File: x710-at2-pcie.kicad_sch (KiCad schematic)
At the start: 16 parts, among them J3 PinHeader_2x3_P2.54mm_SMD, U4 EZX710AT2_S_LMR5

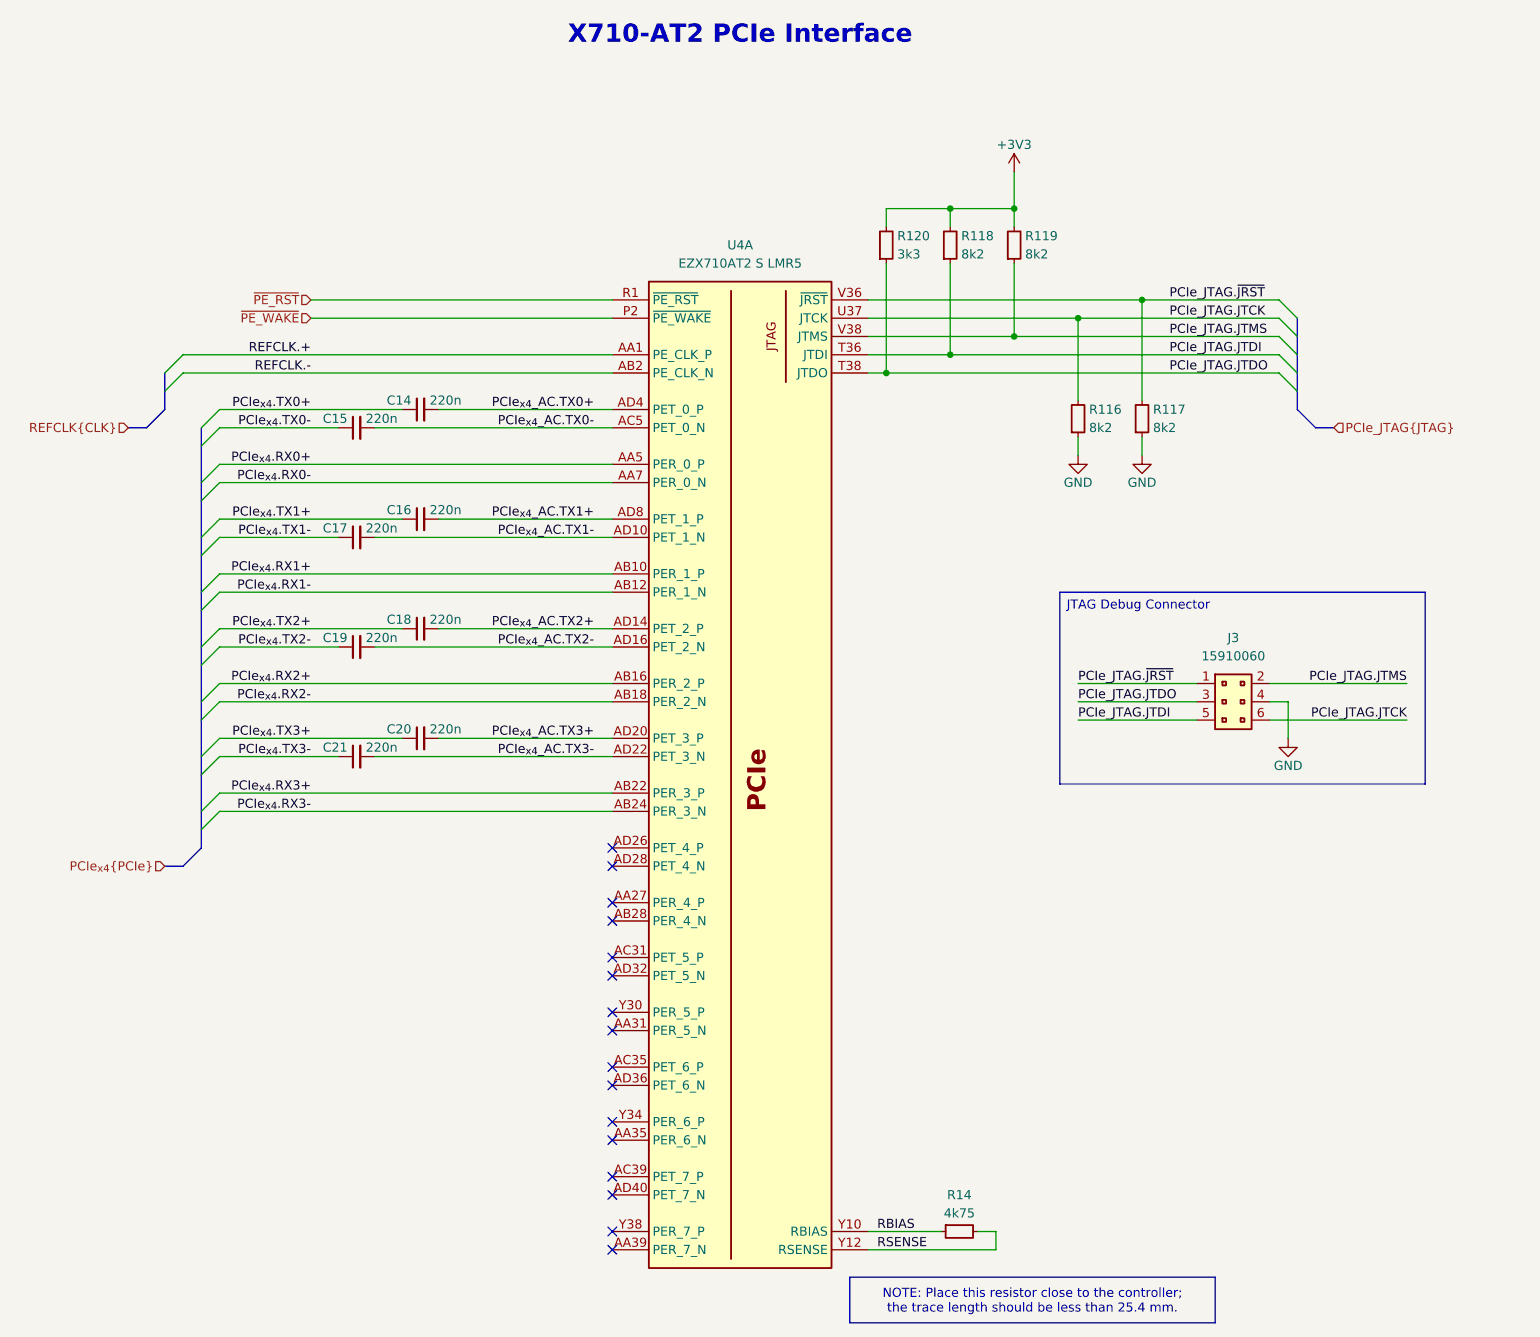
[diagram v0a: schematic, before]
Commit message: [#80813] Add OCuLink connector
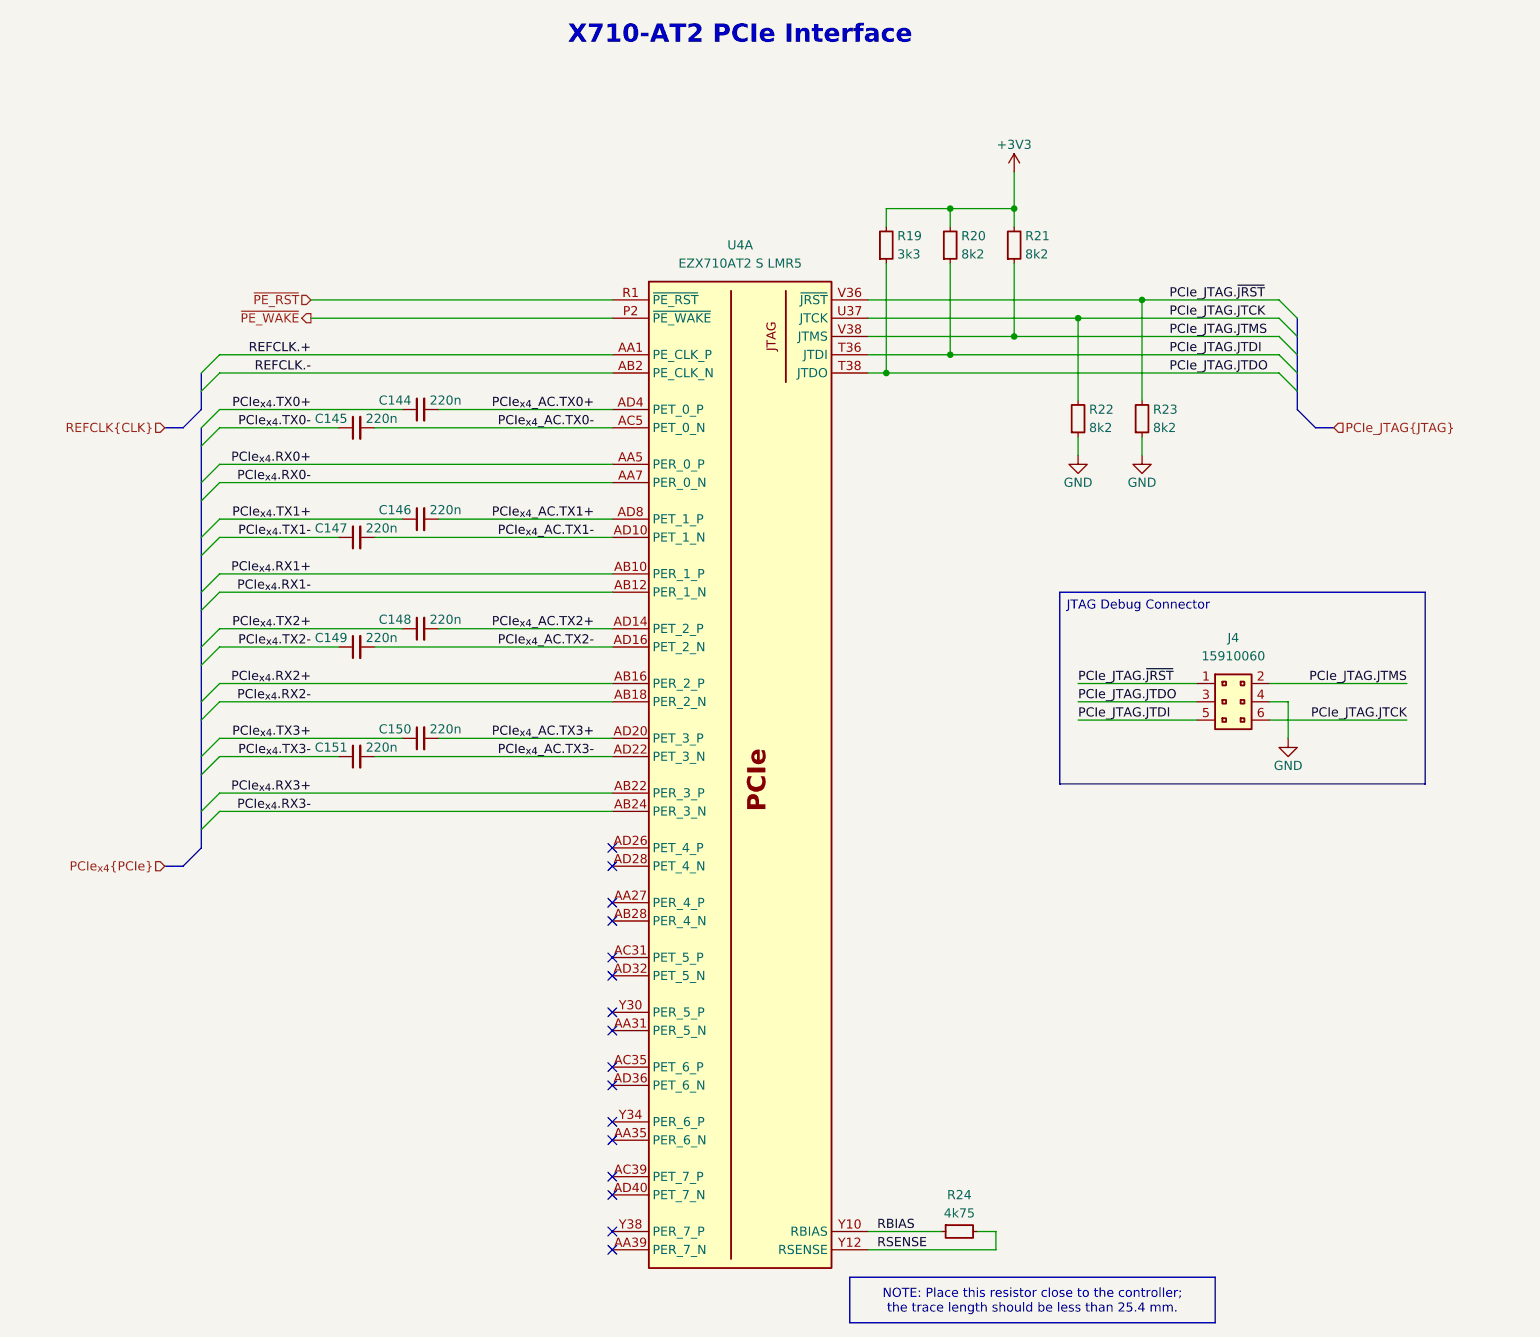
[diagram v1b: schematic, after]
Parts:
- renumbered C14 to C144, C15 to C145, C16 to C146, C17 to C147, C18 to C148, C19 to C149, C20 to C150, C21 to C151, J3 to J4, R120 to R19, R118 to R20, R119 to R21, R116 to R22, R117 to R23, R14 to R24
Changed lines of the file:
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@@
 	)
 	(bus_alias "PCIe"
-		(members "TX7+" "TX7-" "TX6+" "TX6-" "TX5+" "TX5-" "TX4+" "TX4-" "TX3+"
-			"TX3-" "TX2+" "TX2-" "TX1+" "TX1-" "TX0+" "TX0-" "RX7+" "RX7-" "RX6+"
-			"RX6-" "RX5+" "RX5-" "RX4+" "RX4-" "RX3+" "RX3-" "RX2+" "RX2-" "RX1+"
-			"RX1-" "RX0+" "RX0-"
+		(members "TX3+" "TX3-" "TX2+" "TX2-" "TX1+" "TX1-" "TX0+" "TX0-" "RX3+"
+			"RX3-" "RX2+" "RX2-" "RX1+" "RX1-" "RX0+" "RX0-"
 		)
 	)
@@
 	)
 	(bus_entry
-		(at 135.89 97.79)
+		(at 140.97 97.79)
 		(size 2.54 -2.54)
 		(stroke
@@
 	)
 	(bus_entry
-		(at 135.89 100.33)
+		(at 140.97 100.33)
 		(size 2.54 -2.54)
 		(stroke
@@
 	(bus
 		(pts
-			(xy 135.89 97.79) (xy 135.89 100.33)
+			(xy 140.97 97.79) (xy 140.97 100.33)
 		)
 		(stroke
@@
 	(bus
 		(pts
-			(xy 135.89 100.33) (xy 135.89 102.87)
+			(xy 140.97 100.33) (xy 140.97 102.87)
 		)
 		(stroke
@@
 	(wire
 		(pts
-			(xy 138.43 97.79) (xy 198.12 97.79)
+			(xy 143.51 97.79) (xy 198.12 97.79)
 		)
 		(stroke
@@
 	(wire
 		(pts
-			(xy 138.43 95.25) (xy 198.12 95.25)
+			(xy 143.51 95.25) (xy 198.12 95.25)
 		)
 		(stroke
@@
 	(bus
 		(pts
-			(xy 130.81 105.41) (xy 133.35 105.41)
+			(xy 135.89 105.41) (xy 138.43 105.41)
 		)
 		(stroke
@@
 	(bus
 		(pts
-			(xy 133.35 105.41) (xy 135.89 102.87)
+			(xy 138.43 105.41) (xy 140.97 102.87)
 		)
 		(stroke
@@
 	(hierarchical_label "REFCLK{CLK}"
 		(shape input)
-		(at 130.81 105.41 180)
+		(at 135.89 105.41 180)
 		(effects
 			(font
@@
 	)
 	(hierarchical_label "~{PE_WAKE}"
-		(shape input)
+		(shape output)
 		(at 156.21 90.17 180)
 		(effects
@@
 		(polyline
 			(pts
-				(xy 138.43 92.71) (xy 196.85 92.71) (xy 196.85 160.02) (xy 138.43 160.02)
+				(xy 139.7 92.71) (xy 196.85 92.71) (xy 196.85 160.02) (xy 139.7 160.02)
 			)
 			(stroke
@@
 		(length 2.54)
 		(shape round)
-		(at 138.43 92.71 0)
+		(at 139.7 92.71 0)
 		(fields_autoplaced yes)
 		(effects
@@
 		)
 		(property "Netclass" "85Ohm-diff_PCIe"
-			(at 137.7315 90.17 0)
+			(at 139.0015 90.17 0)
 			(effects
 				(font
@@
 		)
 		(property "Component Class" ""
-			(at -85.09 39.37 0)
+			(at -83.82 39.37 0)
 			(effects
 				(font
@@
 		(dnp no)
 		(fields_autoplaced yes)
-		(property "Reference" "J3"
+		(property "Reference" "J4"
 			(at 284.48 134.62 0)
 			(effects
@@
 			(project "10-gbe-expansion"
 				(path "/04bda987-e5eb-48b4-9e90-d8211dc11b39/2e3e9f9b-8e60-4e62-87df-aa866913a2fb"
-					(reference "J3")
+					(reference "J4")
 					(unit 1)
 				)
@@
 		(on_board yes)
 		(dnp no)
-		(property "Reference" "R119"
+		(property "Reference" "R21"
 			(at 255.524 78.74 90)
 			(effects
@@
 			(project "10-gbe-expansion"
 				(path "/04bda987-e5eb-48b4-9e90-d8211dc11b39/2e3e9f9b-8e60-4e62-87df-aa866913a2fb"
-					(reference "R119")
+					(reference "R21")
 					(unit 1)
 				)
@@
 		(on_board yes)
 		(dnp no)
-		(property "Reference" "C20"
+		(property "Reference" "C150"
 			(at 170.18 147.32 0)
 			(effects
@@
 			(project "10-gbe-expansion"
 				(path "/04bda987-e5eb-48b4-9e90-d8211dc11b39/2e3e9f9b-8e60-4e62-87df-aa866913a2fb"
-					(reference "C20")
+					(reference "C150")
 					(unit 1)
 				)
@@
 		(on_board yes)
 		(dnp no)
-		(property "Reference" "#PWR0125"
+		(property "Reference" "#PWR0191"
 			(at 269.24 69.85 0)
 			(effects
@@
 			(project "10-gbe-expansion"
 				(path "/04bda987-e5eb-48b4-9e90-d8211dc11b39/2e3e9f9b-8e60-4e62-87df-aa866913a2fb"
-					(reference "#PWR0125")
+					(reference "#PWR0191")
 					(unit 1)
 				)
@@
 		(on_board yes)
 		(dnp no)
-		(property "Reference" "R14"
+		(property "Reference" "R24"
 			(at 246.38 212.09 0)
 			(effects
@@
 			(project "10-gbe-expansion"
 				(path "/04bda987-e5eb-48b4-9e90-d8211dc11b39/2e3e9f9b-8e60-4e62-87df-aa866913a2fb"
-					(reference "R14")
+					(reference "R24")
 					(unit 1)
 				)
@@
 		(on_board yes)
 		(dnp no)
-		(property "Reference" "C18"
+		(property "Reference" "C148"
 			(at 170.18 132.08 0)
 			(effects
@@
 			(project "10-gbe-expansion"
 				(path "/04bda987-e5eb-48b4-9e90-d8211dc11b39/2e3e9f9b-8e60-4e62-87df-aa866913a2fb"
-					(reference "C18")
+					(reference "C148")
 					(unit 1)
 				)
@@
 		(on_board yes)
 		(dnp no)
-		(property "Reference" "C19"
+		(property "Reference" "C149"
 			(at 161.29 134.62 0)
 			(effects
@@
 			(project "10-gbe-expansion"
 				(path "/04bda987-e5eb-48b4-9e90-d8211dc11b39/2e3e9f9b-8e60-4e62-87df-aa866913a2fb"
-					(reference "C19")
+					(reference "C149")
 					(unit 1)
 				)
@@
 		(on_board yes)
 		(dnp no)
-		(property "Reference" "R118"
+		(property "Reference" "R20"
 			(at 246.634 78.74 90)
 			(effects
@@
 			(project "10-gbe-expansion"
 				(path "/04bda987-e5eb-48b4-9e90-d8211dc11b39/2e3e9f9b-8e60-4e62-87df-aa866913a2fb"
-					(reference "R118")
+					(reference "R20")
 					(unit 1)
 				)
@@
 		(on_board yes)
 		(dnp no)
-		(property "Reference" "C15"
+		(property "Reference" "C145"
 			(at 161.29 104.14 0)
 			(effects
@@
 			(project "10-gbe-expansion"
 				(path "/04bda987-e5eb-48b4-9e90-d8211dc11b39/2e3e9f9b-8e60-4e62-87df-aa866913a2fb"
-					(reference "C15")
+					(reference "C145")
 					(unit 1)
 				)
@@
 		(on_board yes)
 		(dnp no)
-		(property "Reference" "R117"
+		(property "Reference" "R23"
 			(at 273.304 102.87 90)
 			(effects
@@
 			(project "10-gbe-expansion"
 				(path "/04bda987-e5eb-48b4-9e90-d8211dc11b39/2e3e9f9b-8e60-4e62-87df-aa866913a2fb"
-					(reference "R117")
+					(reference "R23")
 					(unit 1)
 				)
@@
 		(on_board yes)
 		(dnp no)
-		(property "Reference" "#PWR0124"
+		(property "Reference" "#PWR0192"
 			(at 271.78 111.76 0)
 			(effects
@@
 			(project "10-gbe-expansion"
 				(path "/04bda987-e5eb-48b4-9e90-d8211dc11b39/2e3e9f9b-8e60-4e62-87df-aa866913a2fb"
-					(reference "#PWR0124")
+					(reference "#PWR0192")
 					(unit 1)
 				)
@@
 		(on_board yes)
 		(dnp no)
-		(property "Reference" "R116"
+		(property "Reference" "R22"
 			(at 264.414 102.87 90)
 			(effects
@@
 			(project ""
 				(path "/04bda987-e5eb-48b4-9e90-d8211dc11b39/2e3e9f9b-8e60-4e62-87df-aa866913a2fb"
-					(reference "R116")
+					(reference "R22")
 					(unit 1)
 				)
@@
 		(on_board yes)
 		(dnp no)
-		(property "Reference" "C17"
+		(property "Reference" "C147"
 			(at 161.29 119.38 0)
 			(effects
@@
 			(project "10-gbe-expansion"
 				(path "/04bda987-e5eb-48b4-9e90-d8211dc11b39/2e3e9f9b-8e60-4e62-87df-aa866913a2fb"
-					(reference "C17")
+					(reference "C147")
 					(unit 1)
 				)
@@
 		(on_board yes)
 		(dnp no)
-		(property "Reference" "C14"
+		(property "Reference" "C144"
 			(at 170.18 101.6 0)
 			(effects
@@
 			(project "10-gbe-expansion"
 				(path "/04bda987-e5eb-48b4-9e90-d8211dc11b39/2e3e9f9b-8e60-4e62-87df-aa866913a2fb"
-					(reference "C14")
+					(reference "C144")
 					(unit 1)
 				)
@@
 		(on_board yes)
 		(dnp no)
-		(property "Reference" "R120"
+		(property "Reference" "R19"
 			(at 237.744 78.74 90)
 			(effects
@@
 			(project ""
 				(path "/04bda987-e5eb-48b4-9e90-d8211dc11b39/2e3e9f9b-8e60-4e62-87df-aa866913a2fb"
-					(reference "R120")
+					(reference "R19")
 					(unit 1)
 				)
@@
 		(on_board yes)
 		(dnp no)
-		(property "Reference" "#PWR0128"
+		(property "Reference" "#PWR0194"
 			(at 300.99 151.13 0)
 			(effects
@@
 			(project "10-gbe-expansion"
 				(path "/04bda987-e5eb-48b4-9e90-d8211dc11b39/2e3e9f9b-8e60-4e62-87df-aa866913a2fb"
-					(reference "#PWR0128")
+					(reference "#PWR0194")
 					(unit 1)
 				)
@@
 		(on_board yes)
 		(dnp no)
-		(property "Reference" "C16"
+		(property "Reference" "C146"
 			(at 170.18 116.84 0)
 			(effects
@@
 			(project "10-gbe-expansion"
 				(path "/04bda987-e5eb-48b4-9e90-d8211dc11b39/2e3e9f9b-8e60-4e62-87df-aa866913a2fb"
-					(reference "C16")
+					(reference "C146")
 					(unit 1)
 				)
@@
 		(on_board yes)
 		(dnp no)
-		(property "Reference" "#PWR0123"
+		(property "Reference" "#PWR0193"
 			(at 280.67 111.76 0)
 			(effects
@@
 			(project "10-gbe-expansion"
 				(path "/04bda987-e5eb-48b4-9e90-d8211dc11b39/2e3e9f9b-8e60-4e62-87df-aa866913a2fb"
-					(reference "#PWR0123")
+					(reference "#PWR0193")
 					(unit 1)
 				)
@@
 		(on_board yes)
 		(dnp no)
-		(property "Reference" "C21"
+		(property "Reference" "C151"
 			(at 161.29 149.86 0)
 			(effects
@@
 			(project "10-gbe-expansion"
 				(path "/04bda987-e5eb-48b4-9e90-d8211dc11b39/2e3e9f9b-8e60-4e62-87df-aa866913a2fb"
-					(reference "C21")
+					(reference "C151")
 					(unit 1)
 				)

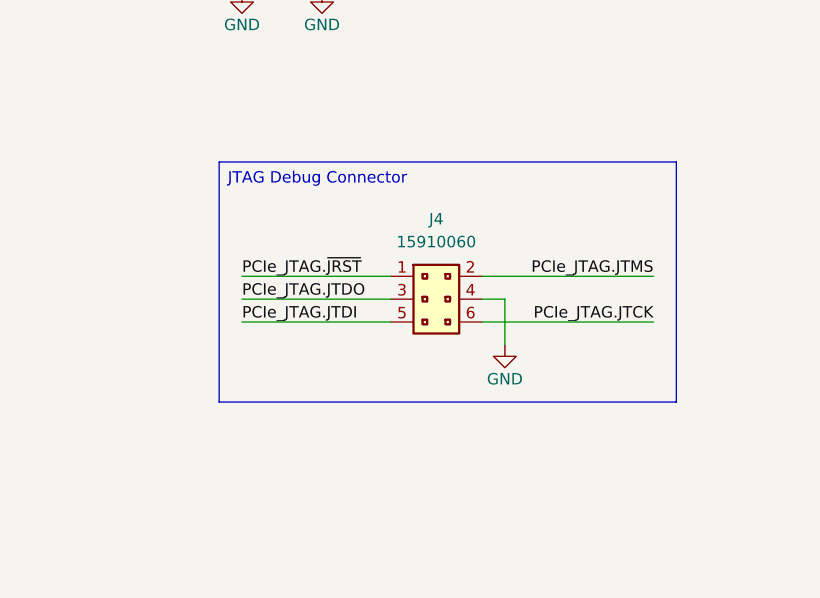
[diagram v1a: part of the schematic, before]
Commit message: [#80813] Add power input connectors, heatsink, mounting, draft component placement
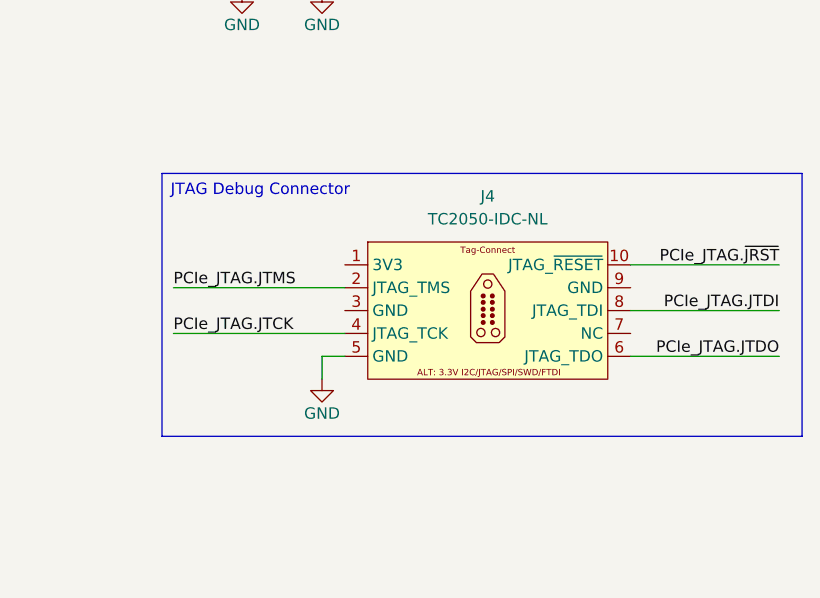
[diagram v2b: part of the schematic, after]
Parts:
- removed J4: PinHeader_2x3_P2.54mm_SMD, antmicro-footprints:PinHeader_2x3_P2.54mm_SMD, symbol antmicroGenericPinHeaders:PinHeader_2x3_P2.54mm_SMD
- added J4: Tag-Connect_TC2050-IDC-NL_2x5_P1.27mm, antmicro-footprints:Tag-Connect_TC2050-IDC-NL_2x5_P1.27mm, symbol antmicroTestPoints:Tag-Connect_TC2050-IDC-NL_2x5_P1.27mm
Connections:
- net GND: now also J4.5
- net PCIe_JTAG.JTCK: now also J4.4
- net PCIe_JTAG.JTDI: now also J4.8
- net PCIe_JTAG.JTDO: now also J4.6
- net PCIe_JTAG.JTMS: now also J4.2
- net PCIe_JTAG.~{JRST}: now also J4.10
